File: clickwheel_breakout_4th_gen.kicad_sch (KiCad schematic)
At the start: 8 parts, among them J1 SFV8R-2STE1HLF, J2 SFV14R-2STE1HLF, J3 SFV8R-2STE1HLF, J4 SFV14R-2STE1HLF, J5 Conn_02x08_Odd_Even, J6 Conn_02x14_Odd_Even, J7 USB_C_Receptacle_USB2.0

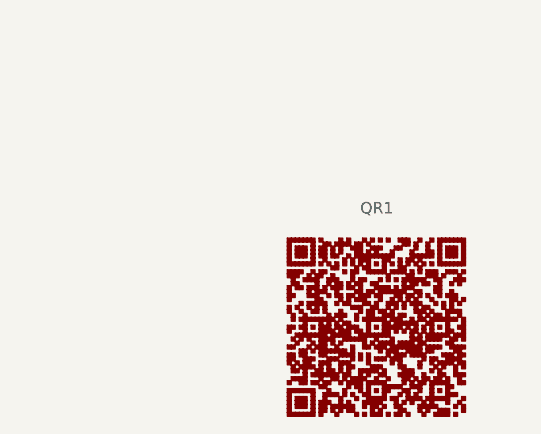
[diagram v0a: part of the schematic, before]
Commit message: fix qr code name
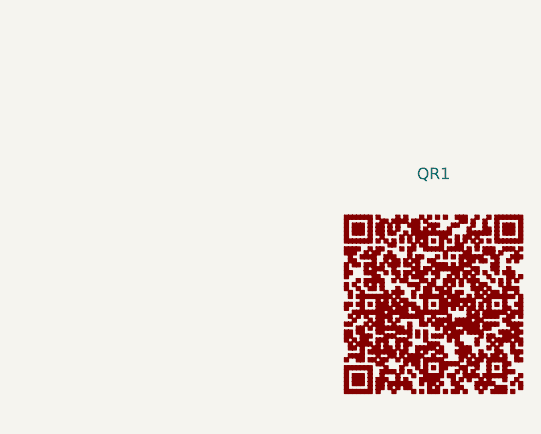
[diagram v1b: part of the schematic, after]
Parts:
- removed QR1: (no value), QR:QR_data, symbol clickwheel_breakout_4th_gen-qr:QR_data
- added QR1: (no value), symbol QR:QR_data
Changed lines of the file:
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@@
     (pin "S1")
   )
-  (symbol (lib_id "clickwheel_breakout_4th_gen-qr:QR_data") (at 254.635 147.955 0) (unit 1)
-    (in_bom no) (on_board yes)
-    (property "Reference" "QR1" (id 0) (at 252.73 134.62 0)
-      (effects (font (size 1.27 1.27)) (justify left))
-    )
-    (property "Value" "" (id 1) (at 250.825 136.525 0)
-      (effects (font (size 1.27 1.27)) (justify left))
-    )
-    (property "Footprint" "QR:QR_data" (id 2) (at 254.635 158.405 0)
+  (symbol (lib_id "QR:QR_data") (at 260.985 145.415 0) (unit 1)
+    (in_bom no) (on_board yes) (fields_autoplaced)
+    (property "Reference" "QR1" (id 0) (at 260.885 130.81 0))
+    (property "Value" "" (id 1) (at 260.885 133.35 0))
+    (property "Footprint" "" (id 2) (at 260.985 158.365 0)
       (effects (font (size 1.27 1.27)) hide)
     )
-    (property "Datasheet" "" (id 3) (at 254.635 160.105 0)
+    (property "Datasheet" "" (id 3) (at 260.985 160.065 0)
       (effects (font (size 1.27 1.27)) hide)
     )
-    (property "qr_version" "7" (id 4) (at 254.635 161.805 0)
+    (property "qr_version" "7" (id 4) (at 260.985 161.765 0)
       (effects (font (size 1.27 1.27)) hide)
     )
-    (property "qr_size" "45" (id 5) (at 254.635 163.505 0)
+    (property "qr_size" "45" (id 5) (at 260.985 163.465 0)
       (effects (font (size 1.27 1.27)) hide)
     )
-    (property "qr_ecc" "0,1" (id 6) (at 254.635 165.205 0)
+    (property "qr_ecc" "0,1" (id 6) (at 260.985 165.165 0)
       (effects (font (size 1.27 1.27)) hide)
     )
-    (property "qr_mask" "3" (id 7) (at 254.635 166.905 0)
+    (property "qr_mask" "3" (id 7) (at 260.985 166.865 0)
       (effects (font (size 1.27 1.27)) hide)
     )
-    (property "qr_text" "OOPSIE WOOPSIE!! Uwu We make a fucky wucky!! A wittle fucko boingo! The code monkeys at our headquarters are working VEWY HAWD to fix this!\n" (id 8) (at 254.635 168.605 0)
+    (property "qr_text" "OOPSIE WOOPSIE!! Uwu We make a fucky wucky!! A wittle fucko boingo! The code monkeys at our headquarters are working VEWY HAWD to fix this!\n" (id 8) (at 260.985 168.565 0)
       (effects (font (size 1.27 1.27)) hide)
     )
@@
       (reference "J7") (unit 1) (value "USB_C_Receptacle_USB2.0") (footprint "Gigahawk:USB_C_Receptacle_GCT_USB4085")
     )
-    (path "/90211c05-3354-414f-a4b4-596a1a6ea313"
+    (path "/e1d122d3-e0b7-44f3-b2d8-4baa56b4ef17"
       (reference "QR1") (unit 1) (value "QR_data") (footprint "QR:QR_data")
     )
